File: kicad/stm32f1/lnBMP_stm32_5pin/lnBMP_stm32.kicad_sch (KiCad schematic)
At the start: 27 parts, among them J1 Debug port, J3 Debug port, J4 USB_OTG, J5 Conn_ARM_JTAG_SWD_10, U1 STM32F103CBTx, U2 LM1117-3.3, Y1 Crystal

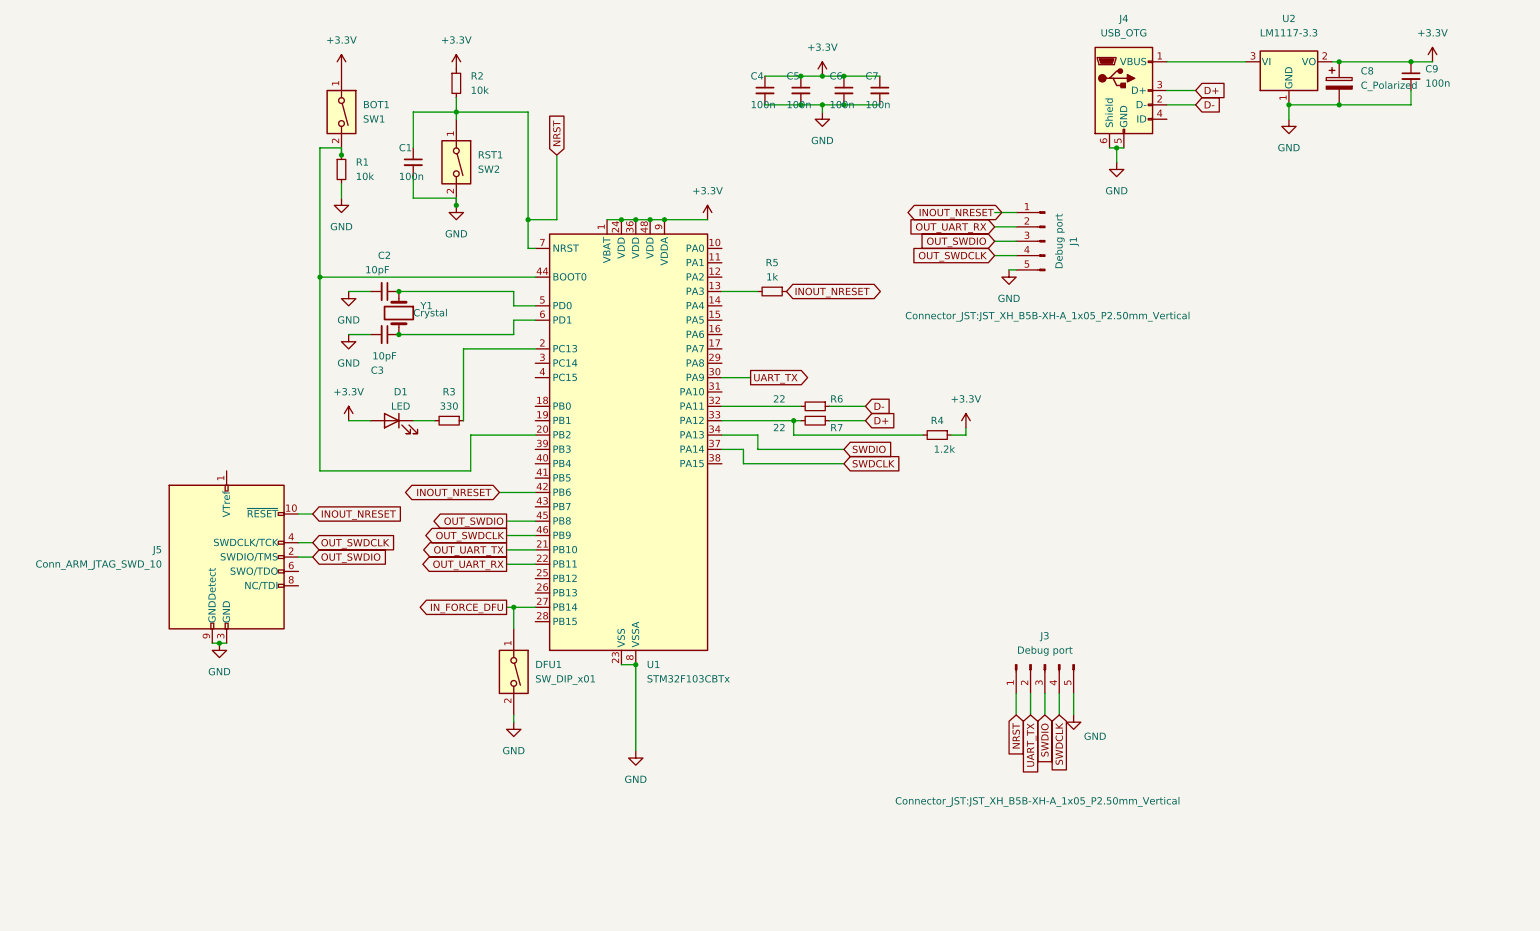
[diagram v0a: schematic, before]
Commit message: kicad : switch to usbC also for stm32/gd32 boards (WIP)
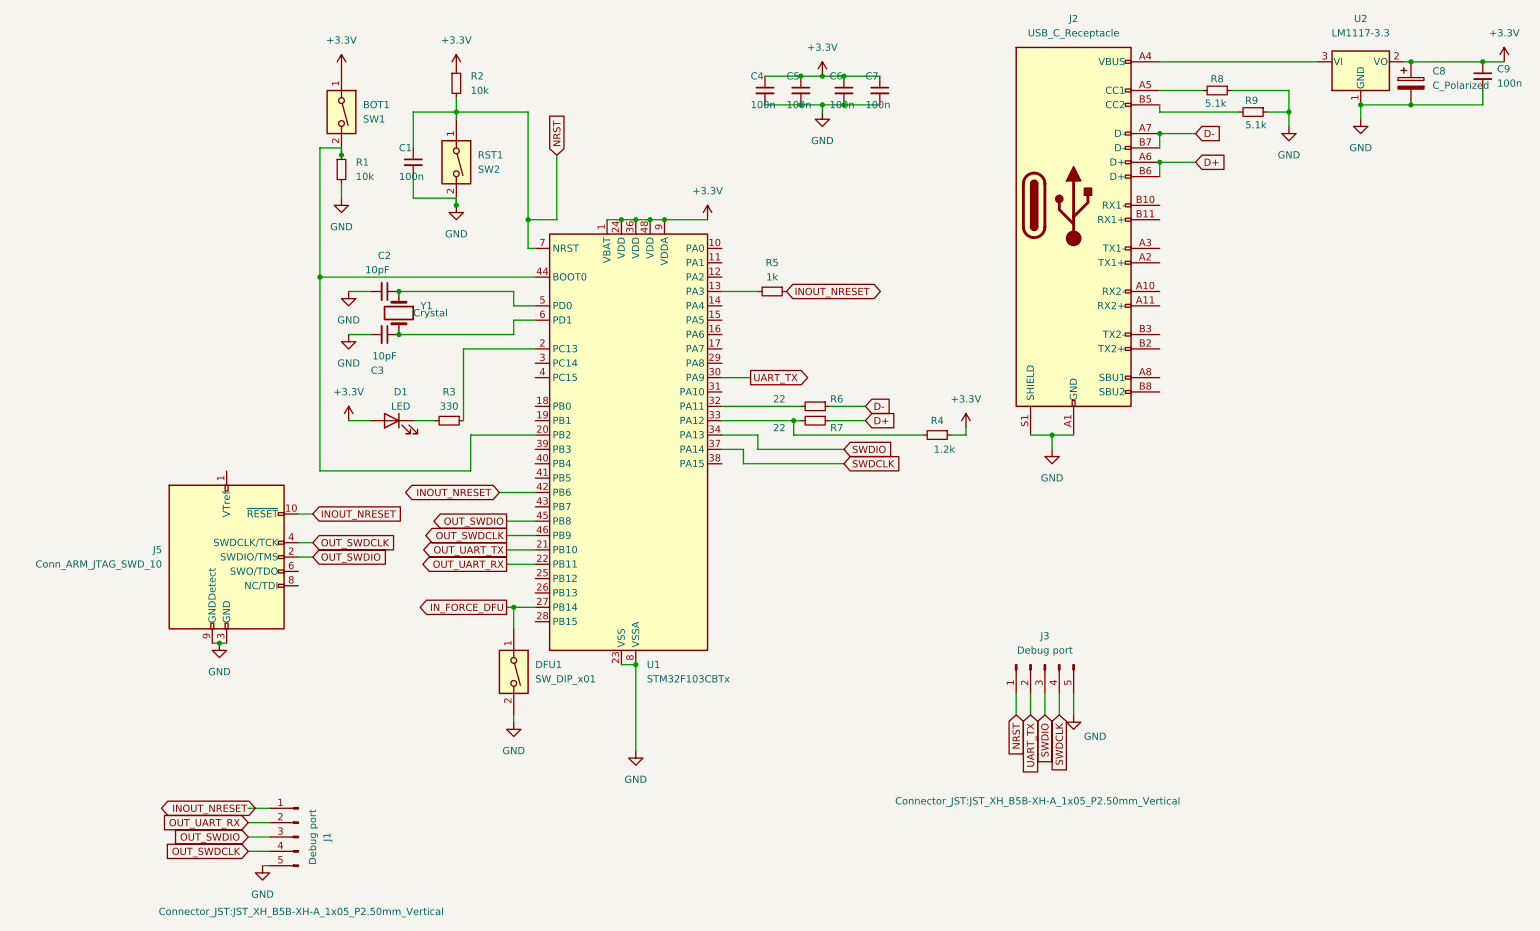
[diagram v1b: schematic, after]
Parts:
- removed J4: USB_OTG, Connector_USB:USB_Micro-B_Wuerth_629105150521, symbol Connector:USB_OTG
- added J2: USB_C_Receptacle, Connector_USB:USB_C_Receptacle_Palconn_UTC16-G, symbol Connector:USB_C_Receptacle
- added R8, R9: 5.1k, Resistor_SMD:R_0603_1608Metric, symbol Device:R_Small
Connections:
- net D+: now also J2.A6 (D+), J2.B6 (D+)
- net D-: now also J2.A7 (D-), J2.B7 (D-)
- net GND: now also J2.A1 (GND), J2.A12 (GND), J2.B1 (GND), J2.B12 (GND), J2.S1 (SHIELD), R8.1, R9.1
- net at U2.3 (VI): now also J2.A4 (VBUS), J2.A9 (VBUS), J2.B4 (VBUS), J2.B9 (VBUS)
- new net: J2.A5 (CC1), R8.2
- new net: J2.B5 (CC2), R9.2
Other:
- moved on the sheet: C8, C9, J1, U2
